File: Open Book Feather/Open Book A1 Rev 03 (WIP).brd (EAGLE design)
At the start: 77.5 x 112.3 mm, 126 parts, among them J1 SJ-43514-SMT, J2 10118193-0001LF, Q1 DMG341, Q2 IRLML0100, SW1 SPDT_SWITCH, U1 AP2112-3.3, U2 MCP73831T-2ACI/OT, U3 ATSAMD51J64-TQFP(10X10), U4 GD25Q16C (or GD25Q32C), U5 MCP23008/SO, U6 GD25Q16C (or GD25Q32C), U8 MAX4466EXK+T, X1 JSTPH, X2 2x5 0.05" SWD

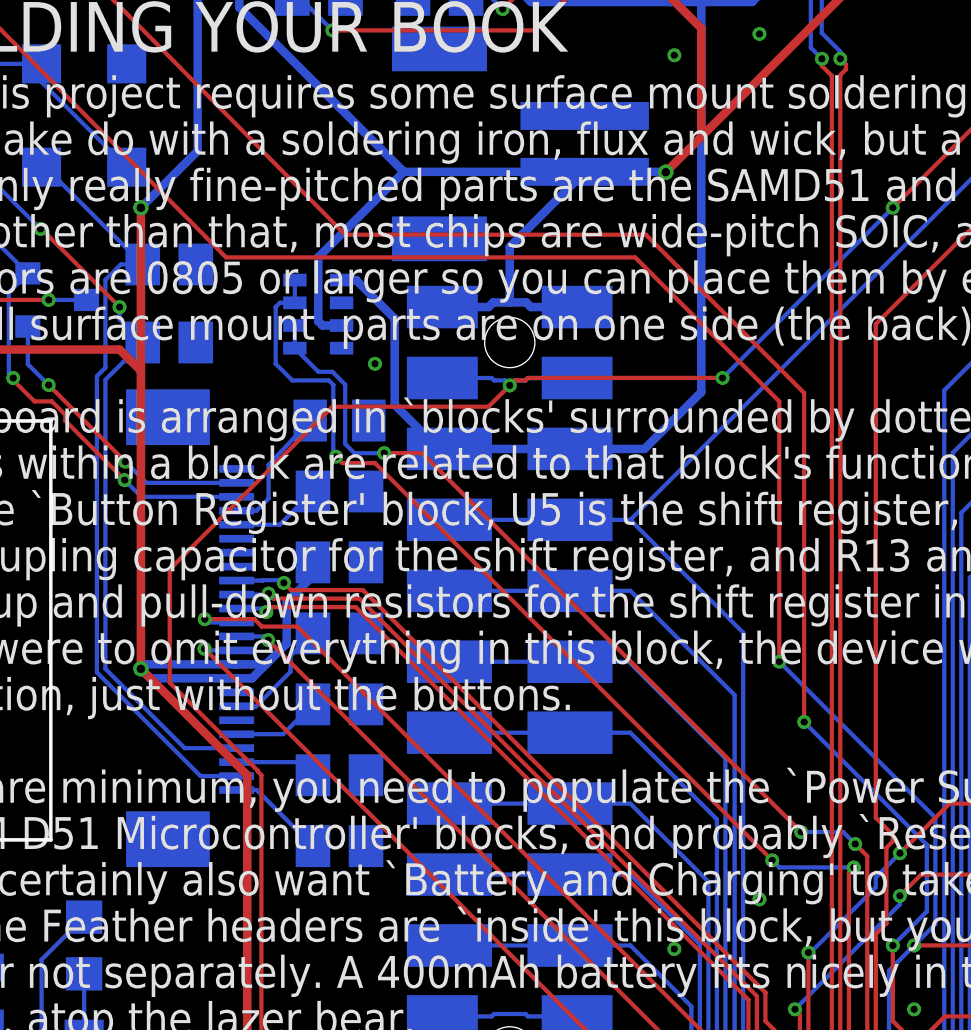
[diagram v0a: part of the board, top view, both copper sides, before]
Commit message: maybe power and gnd pads shouldn't be so close together
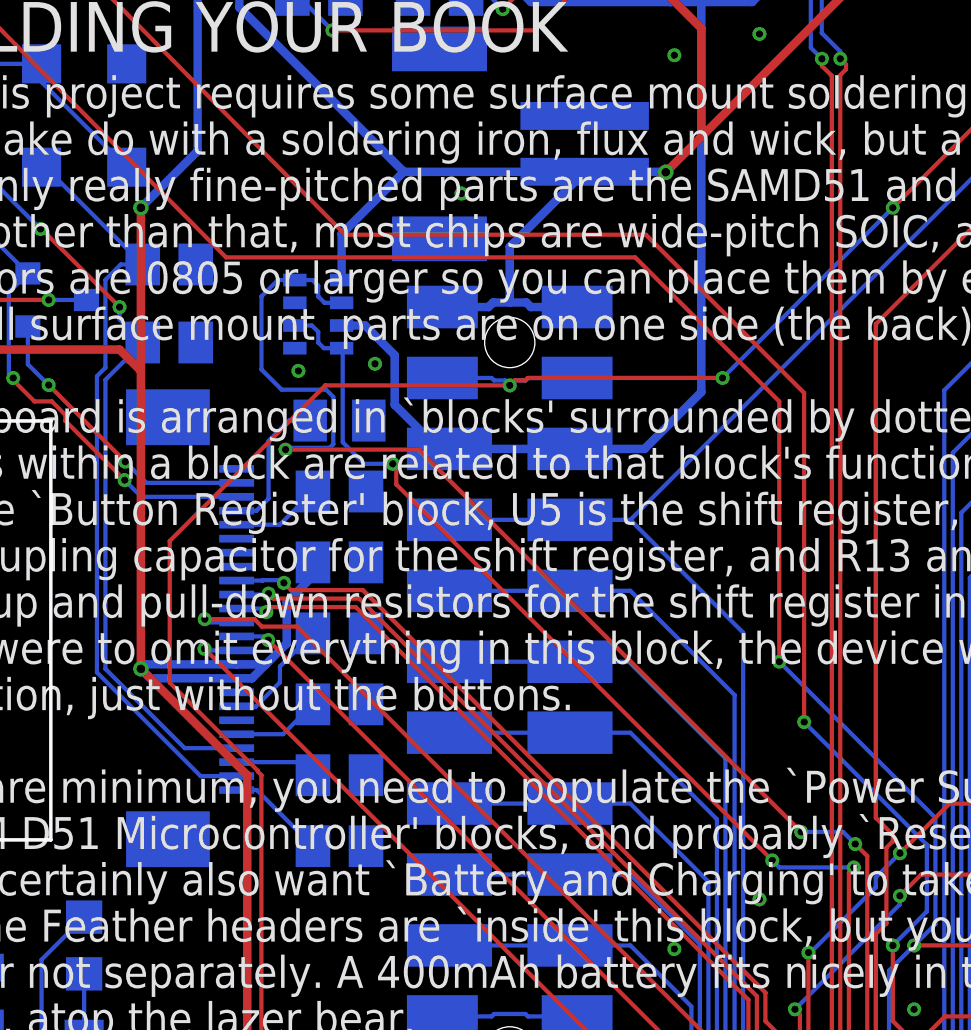
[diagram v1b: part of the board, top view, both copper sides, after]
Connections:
- net A11_VBUSMEAS: now also R9.4, R9.6; no longer R9.7, R9.8
- net A6_VBATMEAS: now also R9.2, R9.8; no longer R9.5, R9.6
- net GND: now also R9.5, R9.7; no longer R9.2, R9.4
- net VBAT: now also R9.1; no longer R9.3
- net VBUS: now also R9.3; no longer R9.1
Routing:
- net A6_VBATMEAS: track 51.3 -> 60.8 mm
- net VBAT: track 71.5 -> 68.8 mm
- net A11_VBUSMEAS: track 54.2 -> 51.5 mm
- net VBUS: track 71.9 -> 70.4 mm
- net EN: track 150.0 -> 150.6 mm
